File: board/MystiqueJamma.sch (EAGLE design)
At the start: 36 parts, among them IC1 7805, IC2 74LS245N, IC3 74LS245N, IC4 74LS245N, IC5 CY7C1049CV33

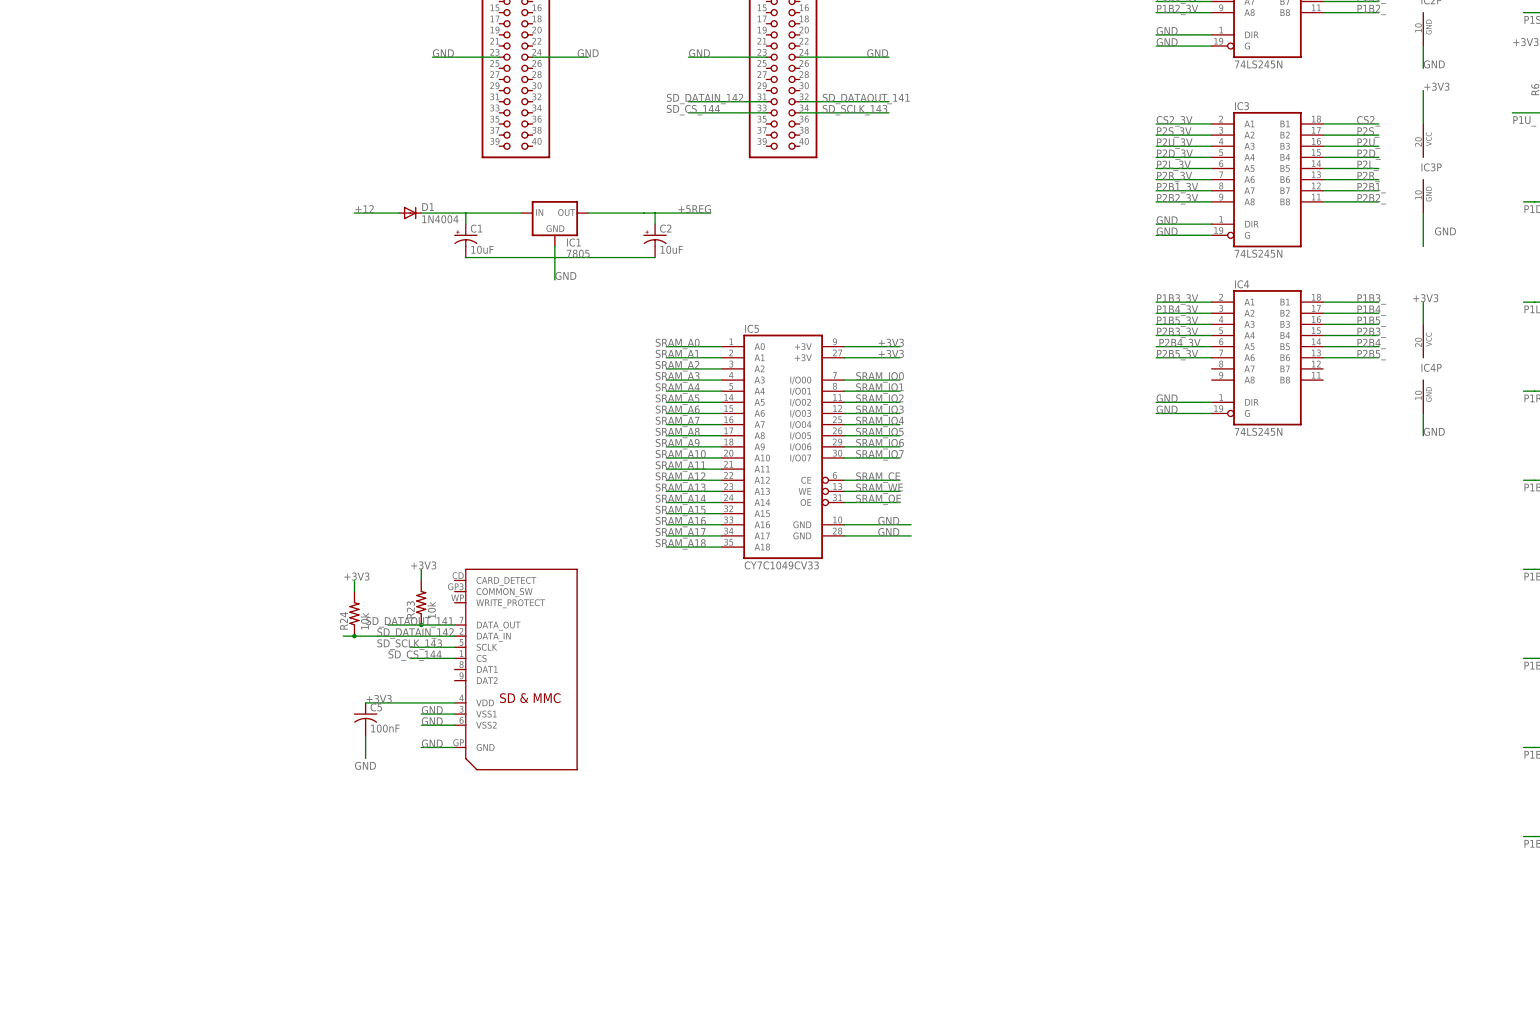
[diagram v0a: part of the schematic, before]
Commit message: changed the jamma connector and included audio TDA1543
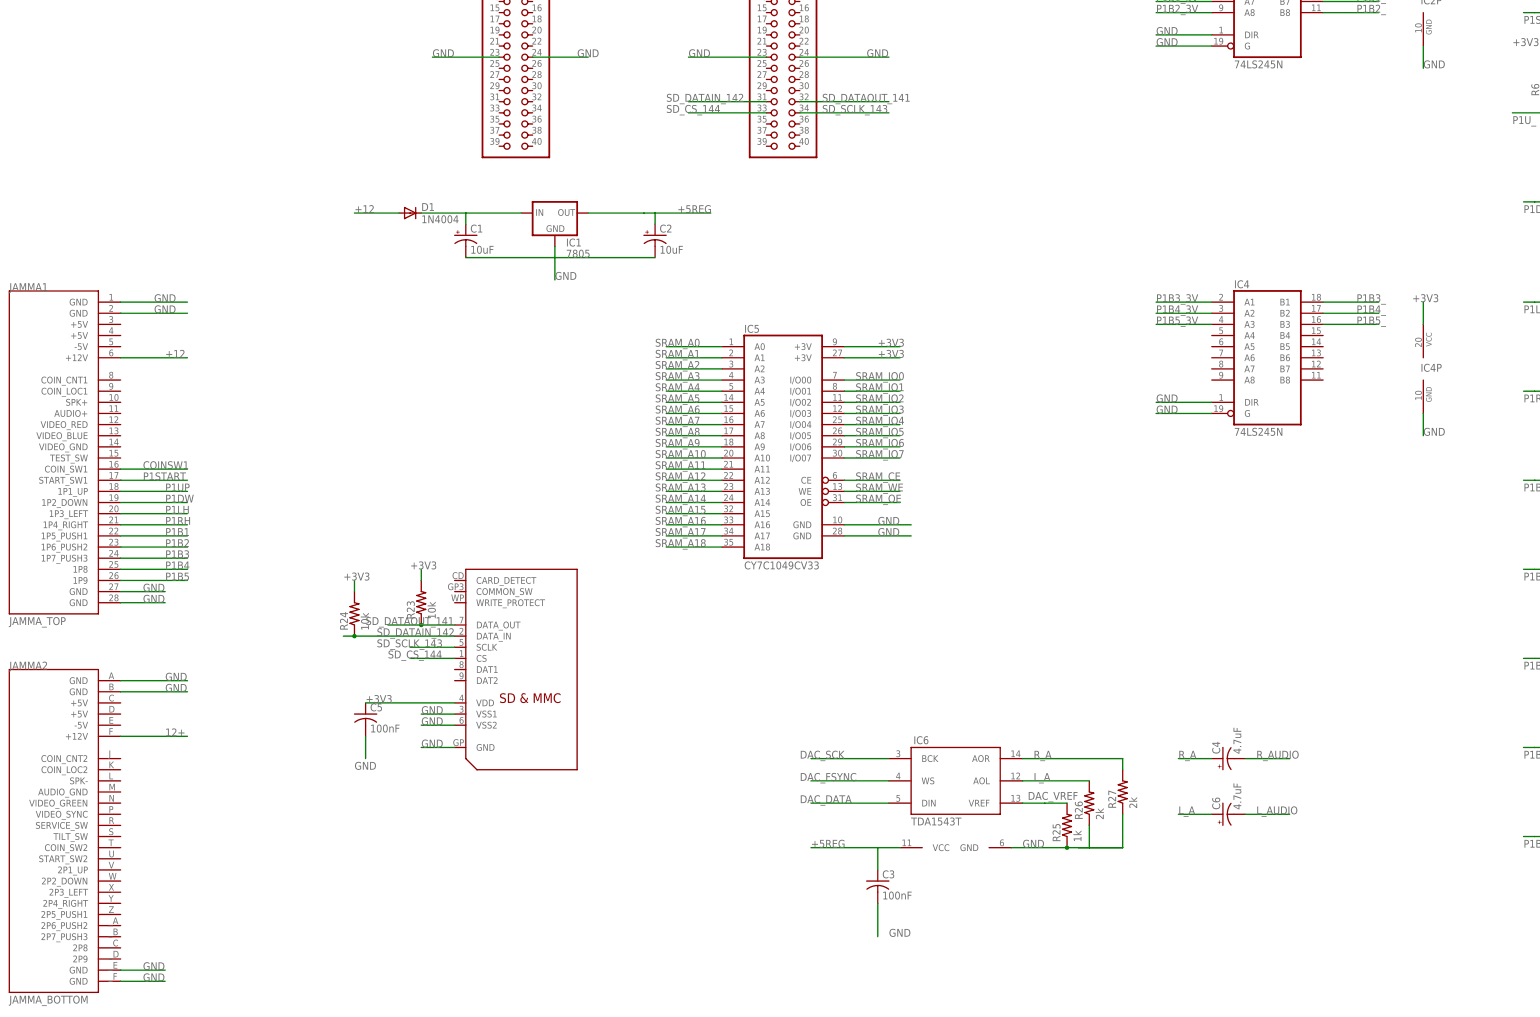
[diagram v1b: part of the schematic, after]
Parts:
- removed IC3: 74LS245N, 74xx-us:74LS245N
- added C3: 100nF, adafruit:C-US025-025X050
- added C4, C6: 4.7uF, adafruit:CPOL-USE5-6
- added IC6: TDA1543T, TDA1543:TDA1543T
- added JAMMA1: JAMMA_TOP, JAMMA:JAMMA_TOP
- added JAMMA2: JAMMA_BOTTOM, JAMMA:JAMMA_BOTTOM
- added R25: 1k, adafruit:R-US_0207/7
- added R26, R27: 2k, adafruit:R-US_0207/7
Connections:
- removed net CS2_: IC3A.B1
- removed net CS2_3V: IC3A.A1
- removed net P2B1_: IC3A.B7
- removed net P2B1_3V: IC3A.A7
- removed net P2B2_: IC3A.B8
- removed net P2B2_3V: IC3A.A8
- removed net P2B3_: IC4A.B4
- removed net P2B3_3V: IC4A.A4
- removed net P2B4_: IC4A.B5
- removed net P2B4_3V: IC4A.A5
- removed net P2B5_: IC4A.B6
- removed net P2B5_3V: IC4A.A6
- removed net P2D_: IC3A.B4
- removed net P2D_3V: IC3A.A4
- removed net P2L_: IC3A.B5
- removed net P2L_3V: IC3A.A5
- removed net P2R_: IC3A.B6
- removed net P2R_3V: IC3A.A6
- removed net P2S_: IC3A.B2
- removed net P2S_3V: IC3A.A2
- removed net P2U_: IC3A.B3
- removed net P2U_3V: IC3A.A3
- new net 12+: JAMMA2.+12V
- new net DAC_DATA: IC6G$1.DIN
- new net DAC_FSYNC: IC6G$1.WS
- new net DAC_SCK: IC6G$1.BCK
- new net DAC_VREF: IC6G$1.VREF, R25.2
- new net L_A: C6.+, IC6G$1.AOL, R26.2
- new net L_AUDIO: C6.-
- new net R_A: C4.+, IC6G$1.AOR, R27.2
- new net R_AUDIO: C4.-
- net +12: now also JAMMA1.+12V
- net +3V3: no longer IC3P.VCC
- net +5REG: now also C3.1, IC6P1.VCC
- net COINSW1: now also JAMMA1.COIN_SW1
- net GND: now also C3.2, IC6P1.GND, JAMMA1.GND@1, JAMMA1.GND@2, JAMMA1.GND@3, JAMMA1.GND@4, JAMMA2.GND@1, JAMMA2.GND@2, JAMMA2.GND@3, JAMMA2.GND@4, R25.1, R26.1, R27.1; no longer IC3A.DIR, IC3A.G, IC3P.GND
- net P1B1: now also JAMMA1.1P5_PUSH1
- net P1B2: now also JAMMA1.1P6_PUSH2
- net P1B3: now also JAMMA1.1P7_PUSH3
- net P1B4: now also JAMMA1.1P8
- net P1B5: now also JAMMA1.1P9
- net P1DW: now also JAMMA1.1P2_DOWN
- net P1LH: now also JAMMA1.1P3_LEFT
- net P1RH: now also JAMMA1.1P4_RIGHT
- net P1START: now also JAMMA1.START_SW1
- net P1UP: now also JAMMA1.1P1_UP

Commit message: audio circuit update
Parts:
- added R28, R29: 1k, adafruit:R-US_0207/7
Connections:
- new net JAMMA_SPK+: JAMMA1.SPK+, R28.2, R29.2
- net GND: now also JAMMA2.SPK-
- net L_AUDIO: now also R29.1
- net R_AUDIO: now also R28.1
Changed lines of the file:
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@@
 <part name="JAMMA1" library="JAMMA" deviceset="JAMMA_TOP" device=""/>
 <part name="JAMMA2" library="JAMMA" deviceset="JAMMA_BOTTOM" device=""/>
+<part name="R28" library="adafruit" deviceset="R-US_" device="0207/7" value="1k"/>
+<part name="R29" library="adafruit" deviceset="R-US_" device="0207/7" value="1k"/>
 </parts>
 <sheets>
@@
 <instance part="JAMMA1" gate="G$1" x="-83.82" y="-33.02"/>
 <instance part="JAMMA2" gate="G$1" x="-86.36" y="-119.38"/>
+<instance part="R28" gate="G$1" x="190.5" y="-134.62"/>
+<instance part="R29" gate="G$1" x="190.5" y="-144.78"/>
 </instances>
 <busses>
@@
 <label x="-66.04" y="-71.12" size="1.778" layer="95"/>
 </segment>
+<segment>
+<pinref part="JAMMA2" gate="G$1" pin="SPK-"/>
+<wire x1="-71.12" y1="-111.76" x2="-55.88" y2="-111.76" width="0.1524" layer="91"/>
+<label x="-60.96" y="-111.76" size="1.778" layer="95"/>
+</segment>
 </net>
 <net name="+12" class="0">
@@
 <label x="187.96" y="-106.68" size="1.778" layer="95"/>
 </segment>
+<segment>
+<wire x1="170.18" y1="-134.62" x2="185.42" y2="-134.62" width="0.1524" layer="91"/>
+<pinref part="R28" gate="G$1" pin="1"/>
+<label x="172.72" y="-134.62" size="1.778" layer="95"/>
+</segment>
 </net>
 <net name="L_AUDIO" class="0">
@@
 <label x="187.96" y="-119.38" size="1.778" layer="95"/>
 </segment>
+<segment>
+<wire x1="170.18" y1="-144.78" x2="185.42" y2="-144.78" width="0.1524" layer="91"/>
+<pinref part="R29" gate="G$1" pin="1"/>
+<label x="172.72" y="-144.78" size="1.778" layer="95"/>
+</segment>
 </net>
 <net name="12+" class="0">
@@
 </segment>
 </net>
+<net name="JAMMA_SPK+" class="0">
+<segment>
+<pinref part="JAMMA1" gate="G$1" pin="SPK+"/>
+<wire x1="-71.12" y1="-25.4" x2="-55.88" y2="-25.4" width="0.1524" layer="91"/>
+<label x="-68.58" y="-25.4" size="1.778" layer="95"/>
+</segment>
+<segment>
+<pinref part="R29" gate="G$1" pin="2"/>
+<wire x1="195.58" y1="-144.78" x2="200.66" y2="-144.78" width="0.1524" layer="91"/>
+<pinref part="R28" gate="G$1" pin="2"/>
+<wire x1="195.58" y1="-134.62" x2="200.66" y2="-134.62" width="0.1524" layer="91"/>
+<wire x1="200.66" y1="-134.62" x2="210.82" y2="-134.62" width="0.1524" layer="91"/>
+<wire x1="200.66" y1="-144.78" x2="200.66" y2="-134.62" width="0.1524" layer="91"/>
+<label x="198.12" y="-134.62" size="1.778" layer="95"/>
+</segment>
+</net>

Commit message: audio circuit
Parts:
- added R30: 20k, adafruit:R-US_0207/7
- R28, R29: value 1k -> 470
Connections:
- net GND: now also R30.1
- net JAMMA_SPK+: now also R30.2
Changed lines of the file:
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@@
 <part name="JAMMA1" library="JAMMA" deviceset="JAMMA_TOP" device=""/>
 <part name="JAMMA2" library="JAMMA" deviceset="JAMMA_BOTTOM" device=""/>
-<part name="R28" library="adafruit" deviceset="R-US_" device="0207/7" value="1k"/>
-<part name="R29" library="adafruit" deviceset="R-US_" device="0207/7" value="1k"/>
+<part name="R28" library="adafruit" deviceset="R-US_" device="0207/7" value="470"/>
+<part name="R29" library="adafruit" deviceset="R-US_" device="0207/7" value="470"/>
+<part name="R30" library="adafruit" deviceset="R-US_" device="0207/7" value="20k"/>
 </parts>
 <sheets>
@@
 <instance part="R28" gate="G$1" x="190.5" y="-134.62"/>
 <instance part="R29" gate="G$1" x="190.5" y="-144.78"/>
+<instance part="R30" gate="G$1" x="200.66" y="-154.94" rot="R90"/>
 </instances>
 <busses>
@@
 <label x="-60.96" y="-111.76" size="1.778" layer="95"/>
 </segment>
+<segment>
+<pinref part="R30" gate="G$1" pin="1"/>
+<wire x1="200.66" y1="-160.02" x2="200.66" y2="-167.64" width="0.1524" layer="91"/>
+<label x="203.2" y="-167.64" size="1.778" layer="95" rot="R90"/>
+</segment>
 </net>
 <net name="+12" class="0">
@@
 <wire x1="200.66" y1="-144.78" x2="200.66" y2="-134.62" width="0.1524" layer="91"/>
 <label x="198.12" y="-134.62" size="1.778" layer="95"/>
-</segment>
-</net>
+<pinref part="R30" gate="G$1" pin="2"/>
+<wire x1="200.66" y1="-149.86" x2="200.66" y2="-144.78" width="0.1524" layer="91"/>
+</segment>
+</net>

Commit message: video circuit
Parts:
- added R31, R32, R33, R34, R35, R39, R40, R41, R42, R43, R47, R48, R49, R50, R51: 2k, adafruit:R-US_0207/7
- added R36, R37, R38, R44, R45, R46, R52, R53, R54: 1k, adafruit:R-US_0207/7
- added R55, R56, R57: 220, adafruit:R-US_0207/7
- added X1: (no value), adafruit:F15HDH
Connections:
- new net JVIDEO_BLUE: JAMMA1.VIDEO_BLUE, R55.2
- new net JVIDEO_GREEN: JAMMA2.VIDEO_GREEN, R56.2
- new net JVIDEO_RED: JAMMA1.VIDEO_RED, R57.2
- new net N$1: R31.1, R32.1, R36.2
- new net N$10: R42.1, R45.1, R46.2
- new net N$11: R47.1, R48.1, R52.2
- new net N$12: R49.1, R52.1, R53.2
- new net N$13: R50.1, R53.1, R54.2
- new net N$3: R33.1, R36.1, R37.2
- new net N$4: X1.8
- new net N$5: X1.7
- new net N$6: X1.6
- new net N$7: R34.1, R37.1, R38.2
- new net N$8: R39.1, R40.1, R44.2
- new net N$9: R41.1, R44.1, R45.2
- new net VGA_B0: R47.2
- new net VGA_B1: R49.2
- new net VGA_B2: R50.2
- new net VGA_B3: R51.2
- new net VGA_BLUE: R51.1, R54.1, R55.1, X1.3
- new net VGA_G0: R39.2
- new net VGA_G1: R41.2
- new net VGA_G2: R42.2
- new net VGA_G3: R43.2
- new net VGA_GREEN: R43.1, R46.1, R56.1, X1.2
- new net VGA_HSYNC: JAMMA2.VIDEO_SYNC, X1.13
- new net VGA_R0: R31.2
- new net VGA_R1: R33.2
- new net VGA_R2: R34.2
- new net VGA_R3: R35.2
- new net VGA_RED: R35.1, R38.1, R57.1, X1.1
- new net VGA_VSYNC: X1.14
- net GND: now also JAMMA1.VIDEO_GND, R32.2, R40.2, R48.2, X1.10, X1.5
